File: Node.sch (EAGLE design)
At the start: 71 parts, among them J1 AVR_SPI_PRG_6NS, J2 M04X2, Q1 PMR280UN, Q2 PMR280UN, Q3 PMR280UN, SW1 KSS, U1 ATMEGA32U4QFN, U2 BLUETOOTH-RN41", U3 LSM303DLM, U4 L3GD20, U9 RCLAMP0502A, X1 USBSMD

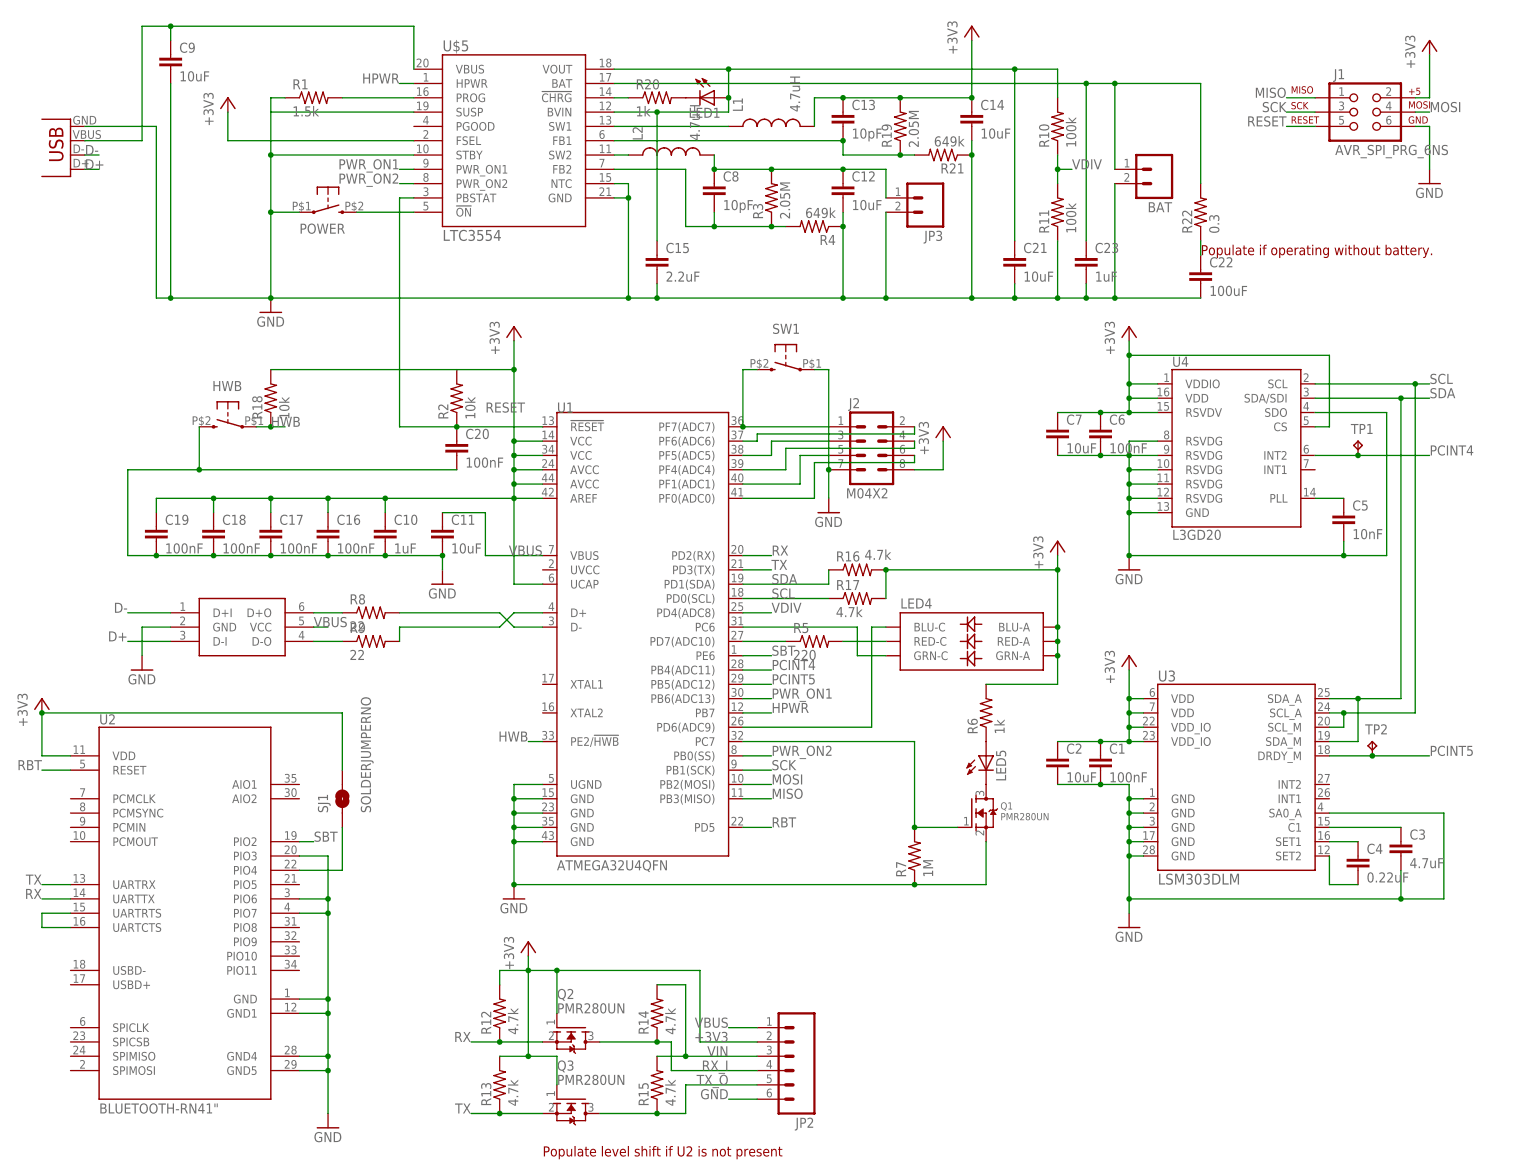
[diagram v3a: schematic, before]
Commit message: swap 32u4 to tfqp, flip battery, LSM303DLHC
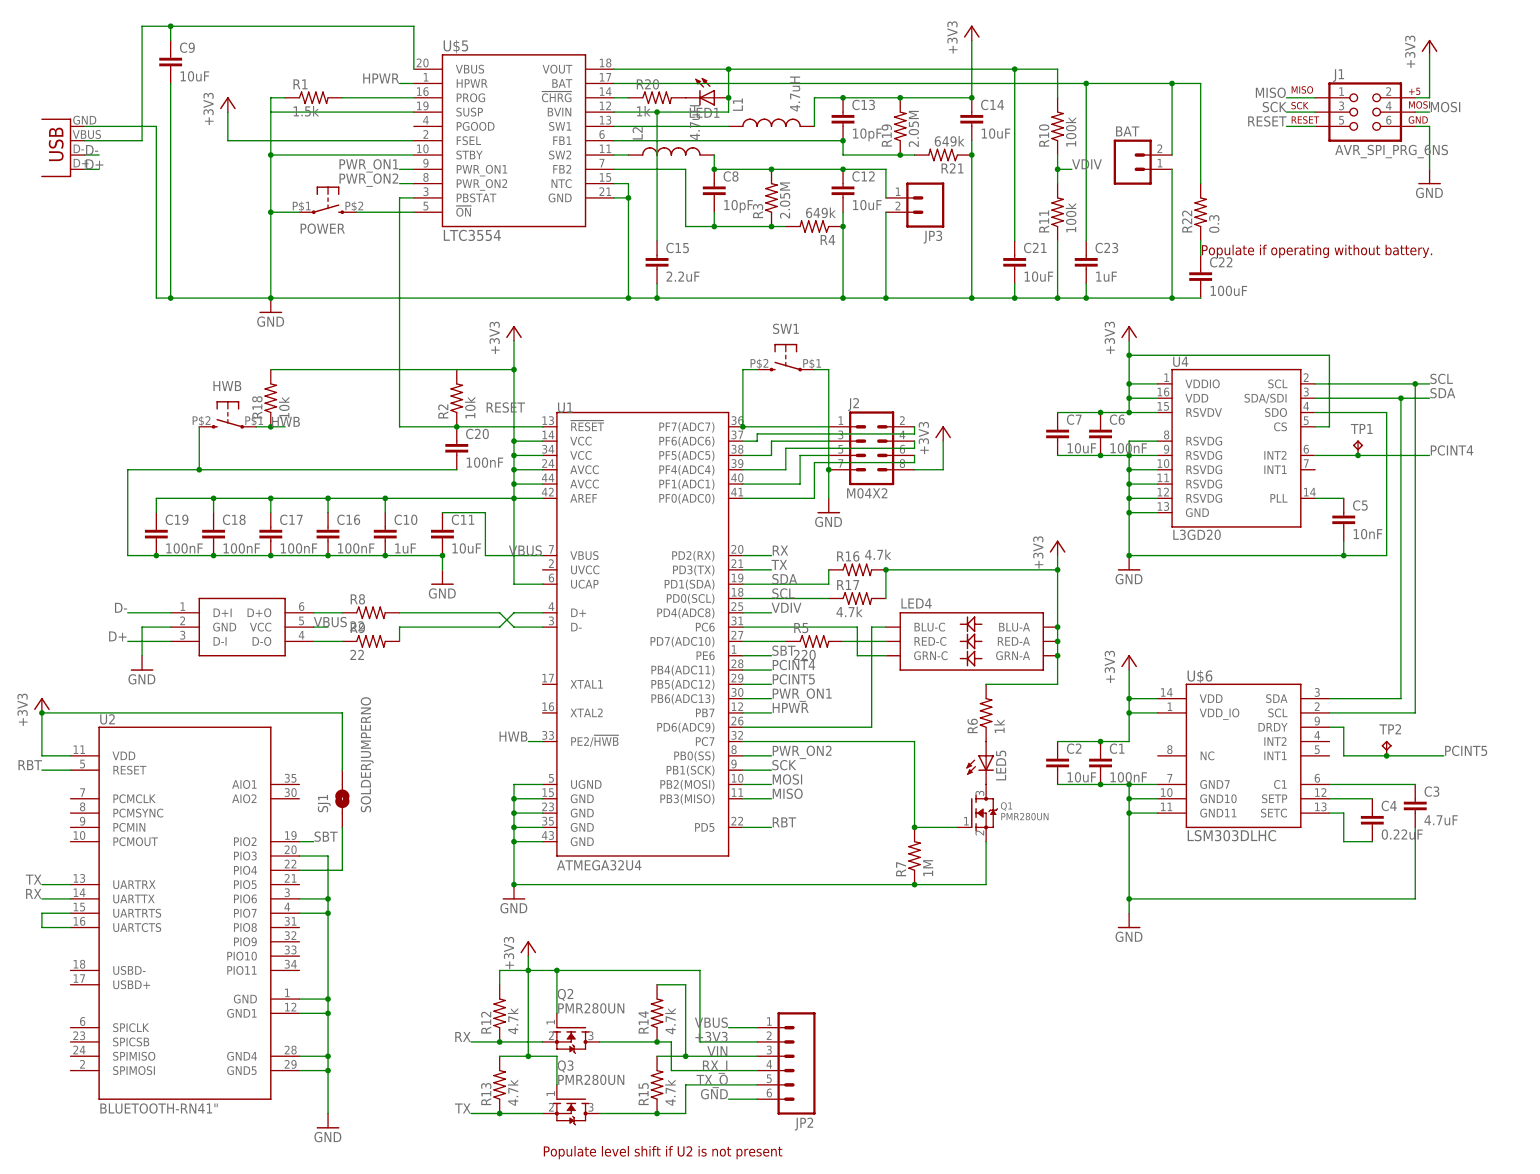
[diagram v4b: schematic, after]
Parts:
- removed U3: LSM303DLM, adjacent-reality:LSM303DLM
- added U$6: LSM303DLHC, adjacent-reality:LSM303DLHC
- U1: value ATMEGA32U4QFN -> ATMEGA32U4; device adjacent-reality:ATMEGA32U4QFN -> adjacent-reality:ATMEGA32U4
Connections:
- net +3V3: now also U$6.VDD, U$6.VDD_IO; no longer U3.VDD, U3.VDD@7, U3.VDD_IO@22, U3.VDD_IO@23
- net GND: now also BAT.1, U$6.GND10, U$6.GND11, U$6.GND7; no longer BAT.2, U3.GND@1, U3.GND@17, U3.GND@2, U3.GND@28, U3.GND@3, U3.SA0_A
- net N$29: now also BAT.2; no longer BAT.1
- net N$3: now also U$6.C1; no longer U3.C1
- net N$5: now also U$6.SETP; no longer U3.SET1
- net N$6: now also U$6.SETC; no longer U3.SET2
- net PCINT5: now also U$6.DRDY; no longer U3.DRDY_M
- net SCL: now also U$6.SCL; no longer U3.SCL_A, U3.SCL_M
- net SDA: now also U$6.SDA; no longer U3.SDA_A, U3.SDA_M
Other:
- moved on the sheet: BAT, C3, C4, TP2

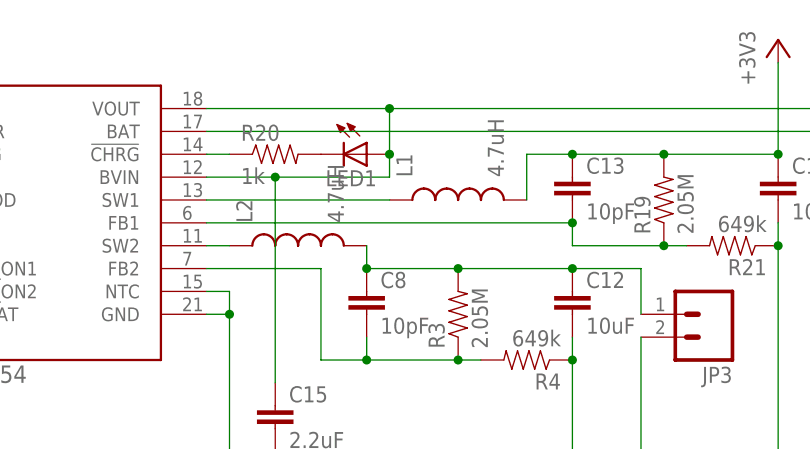
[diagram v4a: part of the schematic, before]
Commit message: add VLS30 inductor package
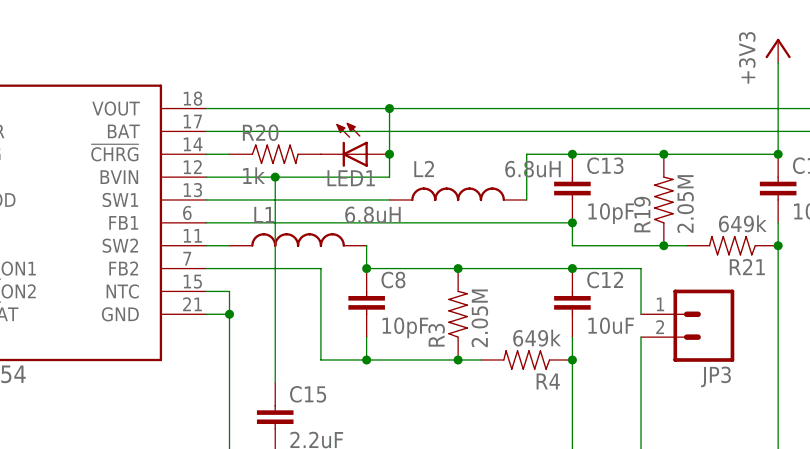
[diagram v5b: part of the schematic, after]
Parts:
- L1, L2: value 4.7uH -> 6.8uH; device SparkFun-Passives:INDUCTOR1210 -> adjacent-reality:INDUCTOR
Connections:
- net +3V3: now also L2.2; no longer L1.2
- net N$19: now also L1.2; no longer L2.2
- net N$23: now also L1.1; no longer L2.1
- net N$27: now also L2.1; no longer L1.1
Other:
- moved on the sheet: L1, L2
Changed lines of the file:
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@@
 <grid distance="0.1" unitdist="inch" unit="inch" style="lines" multiple="1" display="no" altdistance="0.01" altunitdist="inch" altunit="inch"/>
 <layers>
-<layer number="1" name="Top" color="4" fill="1" visible="no" active="no"/>
-<layer number="16" name="Bottom" color="1" fill="1" visible="no" active="no"/>
-<layer number="17" name="Pads" color="2" fill="1" visible="no" active="no"/>
-<layer number="18" name="Vias" color="2" fill="1" visible="no" active="no"/>
-<layer number="19" name="Unrouted" color="6" fill="1" visible="no" active="no"/>
-<layer number="20" name="Dimension" color="15" fill="1" visible="no" active="no"/>
-<layer number="21" name="tPlace" color="7" fill="1" visible="no" active="no"/>
-<layer number="22" name="bPlace" color="7" fill="1" visible="no" active="no"/>
-<layer number="23" name="tOrigins" color="15" fill="1" visible="no" active="no"/>
-<layer number="24" name="bOrigins" color="15" fill="1" visible="no" active="no"/>
-<layer number="25" name="tNames" color="7" fill="1" visible="no" active="no"/>
-<layer number="26" name="bNames" color="7" fill="1" visible="no" active="no"/>
-<layer number="27" name="tValues" color="7" fill="1" visible="no" active="no"/>
-<layer number="28" name="bValues" color="7" fill="1" visible="no" active="no"/>
+<layer number="1" name="Top" color="4" fill="1" visible="yes" active="no"/>
+<layer number="16" name="Bottom" color="1" fill="1" visible="yes" active="no"/>
+<layer number="17" name="Pads" color="2" fill="1" visible="yes" active="no"/>
+<layer number="18" name="Vias" color="2" fill="1" visible="yes" active="no"/>
+<layer number="19" name="Unrouted" color="6" fill="1" visible="yes" active="no"/>
+<layer number="20" name="Dimension" color="15" fill="1" visible="yes" active="no"/>
+<layer number="21" name="tPlace" color="7" fill="1" visible="yes" active="no"/>
+<layer number="22" name="bPlace" color="7" fill="1" visible="yes" active="no"/>
+<layer number="23" name="tOrigins" color="15" fill="1" visible="yes" active="no"/>
+<layer number="24" name="bOrigins" color="15" fill="1" visible="yes" active="no"/>
+<layer number="25" name="tNames" color="7" fill="1" visible="yes" active="no"/>
+<layer number="26" name="bNames" color="7" fill="1" visible="yes" active="no"/>
+<layer number="27" name="tValues" color="7" fill="1" visible="yes" active="no"/>
+<layer number="28" name="bValues" color="7" fill="1" visible="yes" active="no"/>
 <layer number="29" name="tStop" color="7" fill="3" visible="no" active="no"/>
 <layer number="30" name="bStop" color="7" fill="6" visible="no" active="no"/>
@@
 <layer number="35" name="tGlue" color="7" fill="4" visible="no" active="no"/>
 <layer number="36" name="bGlue" color="7" fill="5" visible="no" active="no"/>
-<layer number="37" name="tTest" color="7" fill="1" visible="no" active="no"/>
-<layer number="38" name="bTest" color="7" fill="1" visible="no" active="no"/>
+<layer number="37" name="tTest" color="7" fill="1" visible="yes" active="no"/>
+<layer number="38" name="bTest" color="7" fill="1" visible="yes" active="no"/>
 <layer number="39" name="tKeepout" color="4" fill="11" visible="no" active="no"/>
 <layer number="40" name="bKeepout" color="1" fill="11" visible="no" active="no"/>
@@
 <layer number="44" name="Drills" color="7" fill="1" visible="no" active="no"/>
 <layer number="45" name="Holes" color="7" fill="1" visible="no" active="no"/>
-<layer number="46" name="Milling" color="3" fill="1" visible="no" active="no"/>
-<layer number="47" name="Measures" color="7" fill="1" visible="no" active="no"/>
-<layer number="48" name="Document" color="7" fill="1" visible="no" active="no"/>
-<layer number="49" name="Reference" color="7" fill="1" visible="no" active="no"/>
-<layer number="50" name="dxf" color="7" fill="1" visible="no" active="no"/>
-<layer number="51" name="tDocu" color="7" fill="1" visible="no" active="no"/>
-<layer number="52" name="bDocu" color="7" fill="1" visible="no" active="no"/>
-<layer number="53" name="tGND_GNDA" color="7" fill="9" visible="no" active="no"/>
-<layer number="54" name="bGND_GNDA" color="1" fill="9" visible="no" active="no"/>
-<layer number="56" name="wert" color="7" fill="1" visible="no" active="no"/>
+<layer number="46" name="Milling" color="3" fill="1" visible="yes" active="no"/>
+<layer number="47" name="Measures" color="7" fill="1" visible="yes" active="no"/>
+<layer number="48" name="Document" color="7" fill="1" visible="yes" active="no"/>
+<layer number="49" name="Reference" color="7" fill="1" visible="yes" active="no"/>
+<layer number="50" name="dxf" color="7" fill="1" visible="yes" active="no"/>
+<layer number="51" name="tDocu" color="7" fill="1" visible="yes" active="no"/>
+<layer number="52" name="bDocu" color="7" fill="1" visible="yes" active="no"/>
+<layer number="53" name="tGND_GNDA" color="7" fill="9" visible="yes" active="no"/>
+<layer number="54" name="bGND_GNDA" color="1" fill="9" visible="yes" active="no"/>
+<layer number="56" name="wert" color="7" fill="1" visible="yes" active="no"/>
 <layer number="91" name="Nets" color="2" fill="1" visible="yes" active="yes"/>
 <layer number="92" name="Busses" color="1" fill="1" visible="yes" active="yes"/>
@@
 <part name="R1" library="SparkFun" deviceset="RESISTOR" device="0402-RES" value="1.5k"/>
 <part name="+3V10" library="supply1" deviceset="+3V3" device=""/>
-<part name="L1" library="SparkFun-Passives" deviceset="INDUCTOR" device="1210" value="4.7uH"/>
-<part name="L2" library="SparkFun-Passives" deviceset="INDUCTOR" device="1210" value="4.7uH"/>
 <part name="C8" library="SparkFun" deviceset="CAP" device="0402-CAP" value="10pF"/>
 <part name="R3" library="SparkFun" deviceset="RESISTOR" device="0402-RES" value="2.05M"/>
@@
 <part name="C23" library="SparkFun" deviceset="CAP" device="0402-CAP" value="1uF"/>
 <part name="U$6" library="adjacent-reality" deviceset="LSM303DLHC" device=""/>
+<part name="L1" library="adjacent-reality" deviceset="INDUCTOR" device="" value="6.8uH"/>
+<part name="L2" library="adjacent-reality" deviceset="INDUCTOR" device="" value="6.8uH"/>
 </parts>
 <sheets>
@@
 <instance part="R1" gate="G$1" x="63.5" y="193.04"/>
 <instance part="+3V10" gate="G$1" x="48.26" y="193.04"/>
-<instance part="L1" gate="G$1" x="144.78" y="187.96" rot="R90"/>
-<instance part="L2" gate="G$1" x="127" y="182.88" rot="R90"/>
 <instance part="C8" gate="G$1" x="134.62" y="175.26"/>
 <instance part="R3" gate="G$1" x="144.78" y="175.26" rot="R90"/>
@@
 <instance part="C23" gate="G$1" x="200.66" y="162.56"/>
 <instance part="U$6" gate="G$1" x="228.6" y="76.2"/>
+<instance part="L1" gate="G$1" x="127" y="182.88" smashed="yes" rot="R90">
+<attribute name="NAME" x="121.92" y="185.42" size="1.778" layer="95"/>
+<attribute name="VALUE" x="132.08" y="185.42" size="1.778" layer="96"/>
+</instance>
+<instance part="L2" gate="G$1" x="144.78" y="187.96" smashed="yes" rot="R90">
+<attribute name="NAME" x="139.7" y="190.5" size="1.778" layer="95"/>
+<attribute name="VALUE" x="149.86" y="190.5" size="1.778" layer="96"/>
+</instance>
 </instances>
 <busses>
@@
 <wire x1="157.48" y1="193.04" x2="152.4" y2="193.04" width="0.1524" layer="91"/>
 <wire x1="152.4" y1="193.04" x2="152.4" y2="187.96" width="0.1524" layer="91"/>
-<pinref part="L1" gate="G$1" pin="2"/>
 <pinref part="R19" gate="G$1" pin="2"/>
 <wire x1="157.48" y1="193.04" x2="167.64" y2="193.04" width="0.1524" layer="91"/>
@@
 <junction x="167.64" y="193.04"/>
 <junction x="180.34" y="193.04"/>
+<pinref part="L2" gate="G$1" pin="2"/>
 </segment>
 <segment>
@@
 <net name="N$19" class="0">
 <segment>
-<pinref part="L2" gate="G$1" pin="2"/>
 <pinref part="C8" gate="G$1" pin="1"/>
 <wire x1="134.62" y1="182.88" x2="134.62" y2="180.34" width="0.1524" layer="91"/>
@@
 <wire x1="165.1" y1="180.34" x2="165.1" y2="175.26" width="0.1524" layer="91"/>
 <junction x="157.48" y="180.34"/>
+<pinref part="L1" gate="G$1" pin="2"/>
 </segment>
 </net>
@@
 <segment>
 <pinref part="U$5" gate="G$1" pin="SW2"/>
+<wire x1="116.84" y1="182.88" x2="119.38" y2="182.88" width="0.1524" layer="91"/>
+<pinref part="L1" gate="G$1" pin="1"/>
+</segment>
+</net>
+<net name="N$27" class="0">
+<segment>
+<pinref part="U$5" gate="G$1" pin="SW1"/>
+<wire x1="116.84" y1="187.96" x2="137.16" y2="187.96" width="0.1524" layer="91"/>
 <pinref part="L2" gate="G$1" pin="1"/>
-<wire x1="116.84" y1="182.88" x2="119.38" y2="182.88" width="0.1524" layer="91"/>
-</segment>
-</net>
-<net name="N$27" class="0">
-<segment>
-<pinref part="U$5" gate="G$1" pin="SW1"/>
-<pinref part="L1" gate="G$1" pin="1"/>
-<wire x1="116.84" y1="187.96" x2="137.16" y2="187.96" width="0.1524" layer="91"/>
-</segment>
-</net>
+</segment>
+</net>

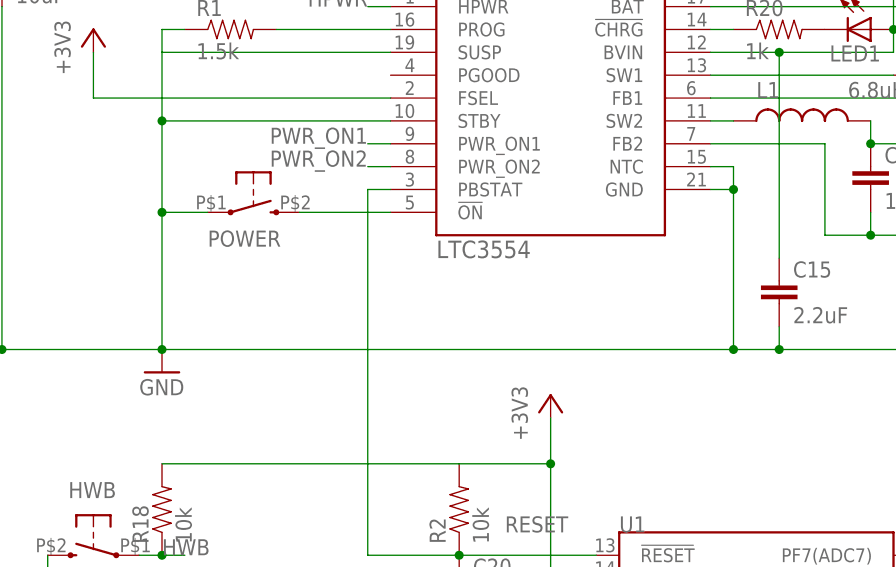
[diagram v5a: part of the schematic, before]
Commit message: add header for power button
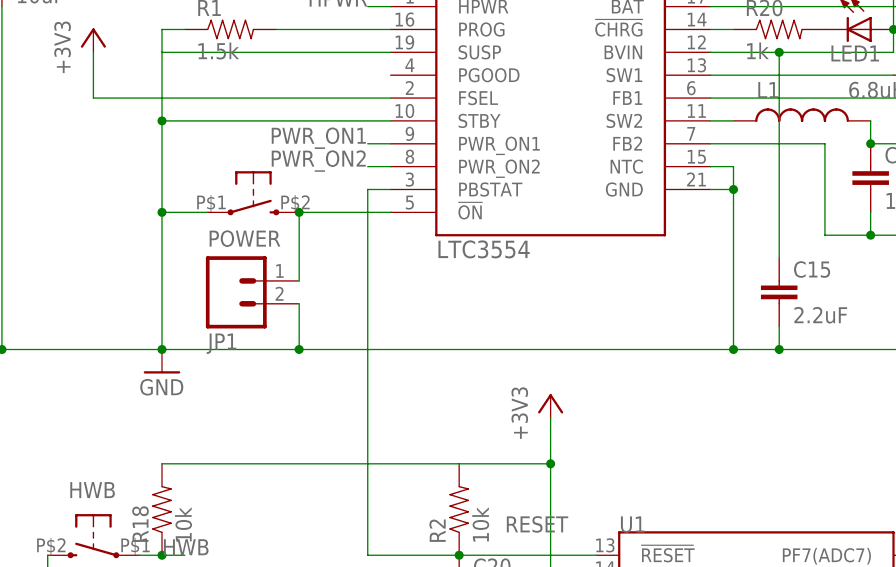
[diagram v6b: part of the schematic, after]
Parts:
- added JP1: (no value), SparkFun-Connectors:M02PTH
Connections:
- net GND: now also JP1.2
- net N$8: now also JP1.1
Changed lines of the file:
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@@
 <part name="L1" library="adjacent-reality" deviceset="INDUCTOR" device="" value="6.8uH"/>
 <part name="L2" library="adjacent-reality" deviceset="INDUCTOR" device="" value="6.8uH"/>
+<part name="JP1" library="SparkFun-Connectors" deviceset="M02" device="PTH"/>
 </parts>
 <sheets>
@@
 <attribute name="VALUE" x="149.86" y="190.5" size="1.778" layer="96"/>
 </instance>
+<instance part="JP1" gate="G$1" x="63.5" y="165.1" rot="MR180"/>
 </instances>
 <busses>
@@
 <junction x="55.88" y="157.48"/>
 <wire x1="38.1" y1="157.48" x2="55.88" y2="157.48" width="0.1524" layer="91"/>
-<wire x1="55.88" y1="157.48" x2="119.38" y2="157.48" width="0.1524" layer="91"/>
+<wire x1="55.88" y1="157.48" x2="71.12" y2="157.48" width="0.1524" layer="91"/>
+<wire x1="71.12" y1="157.48" x2="119.38" y2="157.48" width="0.1524" layer="91"/>
 <wire x1="187.96" y1="157.48" x2="195.58" y2="157.48" width="0.1524" layer="91"/>
 <pinref part="R11" gate="G$1" pin="1"/>
@@
 <wire x1="215.9" y1="180.34" x2="215.9" y2="157.48" width="0.1524" layer="91"/>
 <junction x="215.9" y="157.48"/>
+<pinref part="JP1" gate="G$1" pin="2"/>
+<wire x1="71.12" y1="162.56" x2="71.12" y2="157.48" width="0.1524" layer="91"/>
+<junction x="71.12" y="157.48"/>
 </segment>
 <segment>
@@
 <pinref part="U$5" gate="G$1" pin="!ON"/>
 <wire x1="71.12" y1="172.72" x2="81.28" y2="172.72" width="0.1524" layer="91"/>
-</segment>
-</net>
+<pinref part="JP1" gate="G$1" pin="1"/>
+<wire x1="71.12" y1="165.1" x2="71.12" y2="172.72" width="0.1524" layer="91"/>
+<junction x="71.12" y="172.72"/>
+</segment>
+</net>
